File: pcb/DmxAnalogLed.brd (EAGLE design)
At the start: 37 parts, among them J1 RS485, J2 POWER_JACKPTH, J3 RS485, Q1 16MHz 10ppm, U1 ARDUINO_LEONARDO-REV3B_SMARTP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, U2 SN75176ASOIC, X1 USBPTH

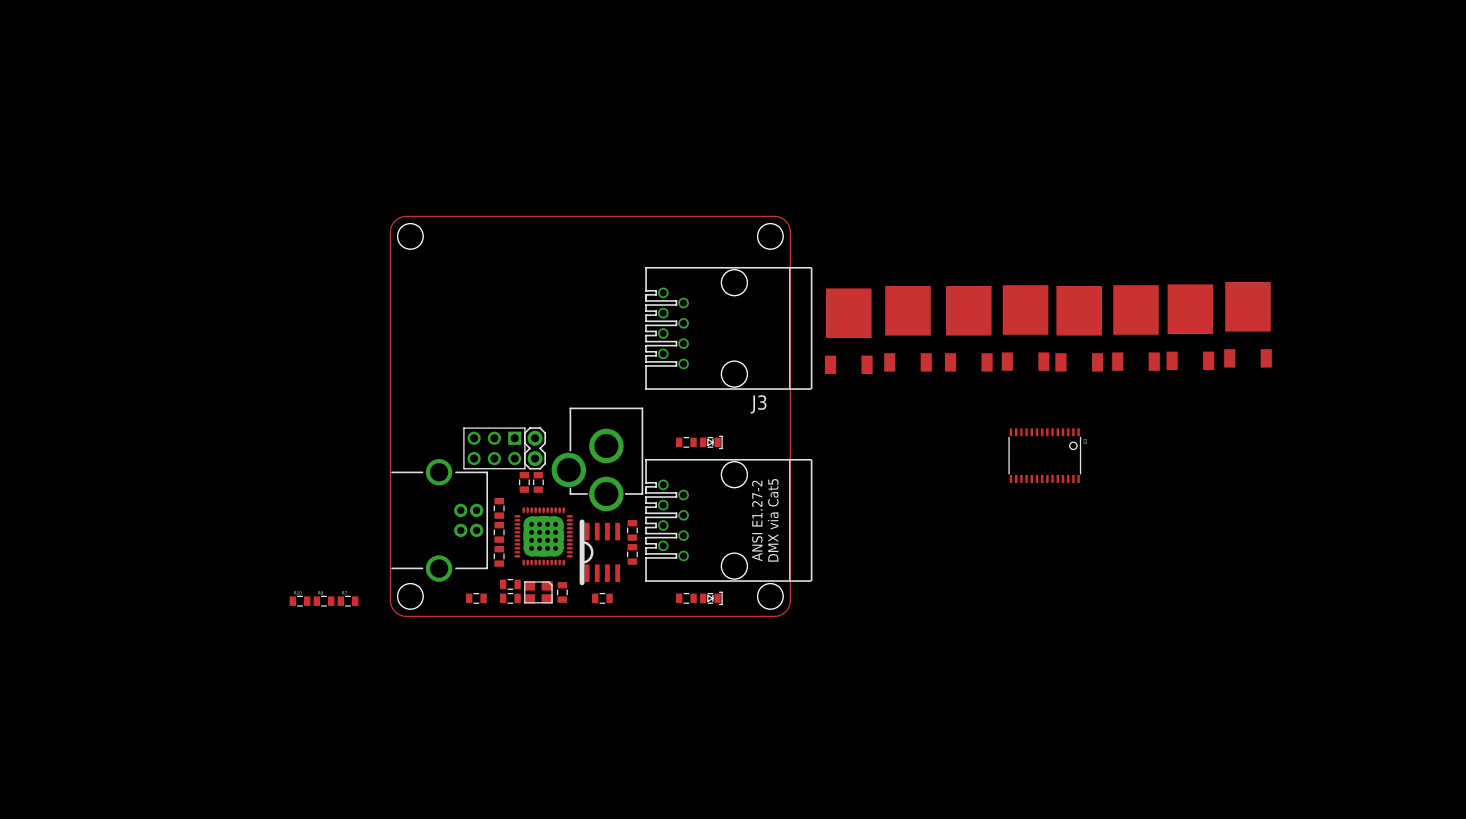
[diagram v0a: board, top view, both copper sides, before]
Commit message: Add isolated RS485 circuit, begin transistor layout
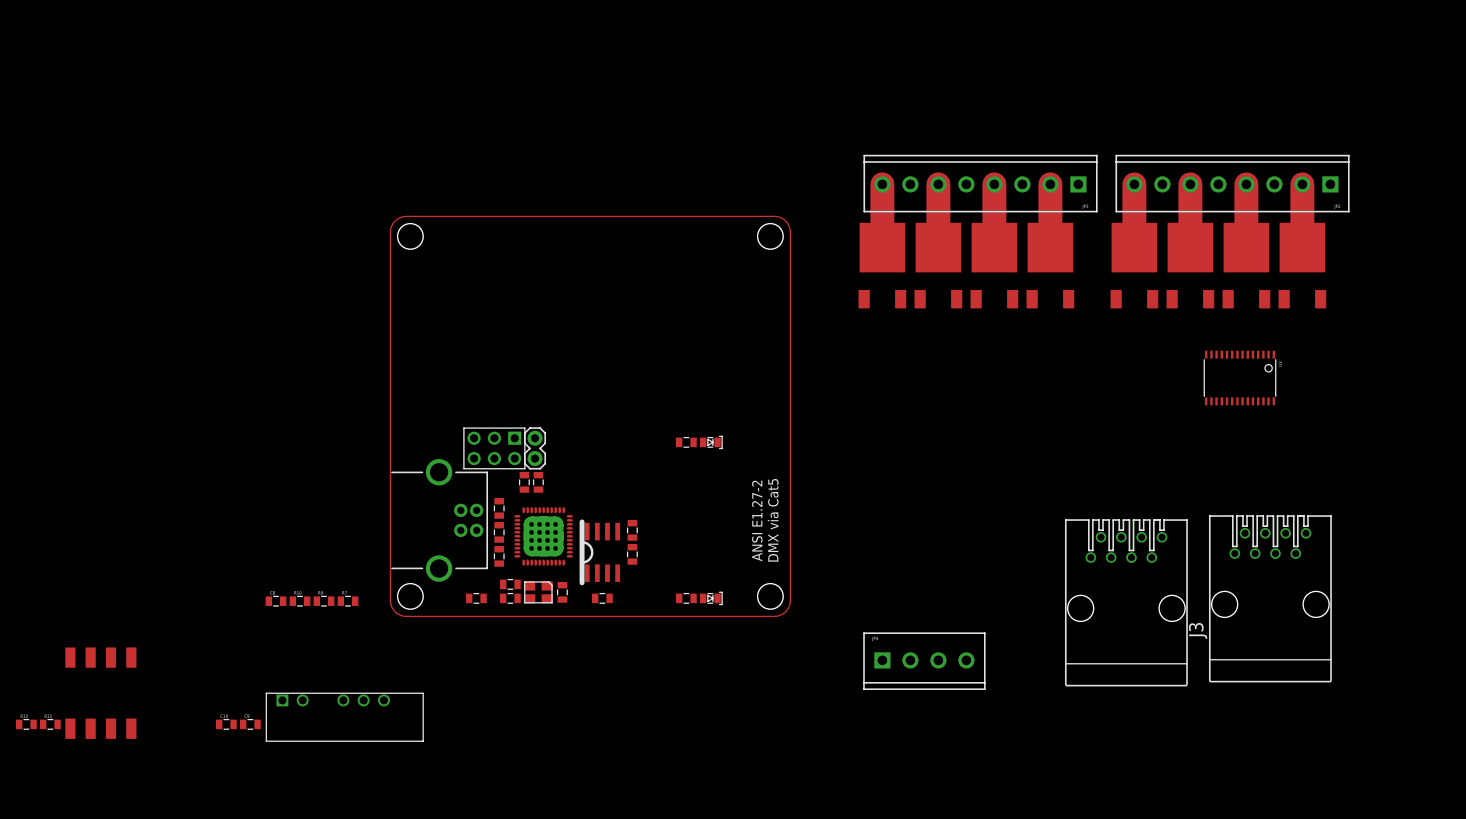
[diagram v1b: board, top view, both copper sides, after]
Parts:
- removed J2: POWER_JACKPTH, SparkFun:POWER_JACK_PTH
- added C10: 10uF, SparkFun:0805
- added C8: 100nF, SparkFun:0805
- added C9: 4.7uF, SparkFun:0805
- added JP2, JP3: (no value), SparkFun:SCREWTERMINAL-3.5MM-8
- added JP4: (no value), SparkFun:SCREWTERMINAL-3.5MM-4
- added R11, R12: 470, SparkFun:0805
- added U$10: DC_DC_ISOLATED_0505, blinkiverse:IB_XLS-1W
- added U$12: 6N137, sonos_library:8_SOIC
- moved J3 75.4 mm to (110.0, 1.50), turned to 0 degrees
- moved J1 50.2 mm to (92.0, 1.00), turned to 0 degrees
- moved U3 26.3 mm to (106.2, 29.8)
- moved U$5 10.5 mm to (93.0, 43.0)
- moved U$3 10.4 mm to (107.0, 43.0)
- moved U$4 10.3 mm to (100.0, 43.0)
- moved U$1 10.0 mm to (114.0, 43.0)
- moved U$9 9.21 mm to (61.5, 43.0)
- moved U$8 8.77 mm to (68.5, 43.0)
- moved U$7 8.52 mm to (75.5, 43.0)
- moved U$6 8.39 mm to (82.5, 43.0)
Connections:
- new net 5V_ISO: C10.2, C7.2, U$10.P$5, U$12.P$2, U2.8
- new net GND_ISO: C10.1, C7.1, J1.7, J1.8, J3.7, J3.8, R2.2, U$10.P$3, U$10.P$4, U2.5
- new net N$10: JP4.1, JP4.2
- new net N$13: JP4.3, JP4.4
- new net N$14: R11.1, U$12.P$3
- new net RX_ISO: R11.2, U2.1
- new net V_LED: JP2.1, JP2.3, JP2.5, JP2.7, JP3.1, JP3.3, JP3.5, JP3.7
- net GND: now also C8.1, C9.1, U$10.P$2, U$12.P$5; no longer C7.1, J1.7, J1.8, J2.GND, J2.GNDBREAK, J3.7, J3.8, R2.2, U2.5, U3.2
- net OUT0: now also JP2.2
- net OUT1: now also JP2.4
- net OUT2: now also JP2.6
- net OUT3: now also JP2.8
- net OUT4: now also JP3.2
- net OUT5: now also JP3.4
- net OUT6: now also JP3.6
- net OUT7: now also JP3.8
- net RX: no longer U2.1
- net TX: now also R12.1, U$12.P$6; no longer U2.4
- net VCC: now also C8.2, C9.2, R12.2, U$10.P$1, U$12.P$8, U3.2; no longer C7.2, U2.8
- net VMOT: no longer J2.PWR
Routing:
- net OUT7: track 0.00 -> 7.90 mm
- net OUT6: track 0.00 -> 7.90 mm
- net OUT5: track 0.00 -> 7.90 mm
- net OUT4: track 0.00 -> 7.90 mm
- net OUT3: track 0.00 -> 7.90 mm
- net OUT2: track 0.00 -> 7.90 mm
- net OUT1: track 0.00 -> 7.90 mm
- net OUT0: track 0.00 -> 7.90 mm

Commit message: Board update
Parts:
- moved R12 155.2 mm to (107.0, 15.5), turned to 90 degrees
- moved R11 151.7 mm to (107.0, 12.0), turned to 90 degrees
- moved U$12 151.3 mm to (109.5, 11.5)
- moved C10 117.8 mm to (93.5, 16.0)
- moved C9 104.7 mm to (83.0, 16.0), turned to 180 degrees
- moved U$10 98.5 mm to (82.0, 13.5)
- moved C7 88.2 mm to (106.2, 8.00), turned to 180 degrees
- moved R2 77.4 mm to (102.0, 19.2)
- moved U2 76.2 mm to (102.5, 13.5), turned to 180 degrees
- moved R1 72.5 mm to (102.8, 8.25), turned to 0 degrees
- moved C5 9.90 mm to (23.2, 17.8), turned to 180 degrees
- moved J3 6.02 mm to (109.5, -4.50)
- moved J1 5.50 mm to (92.0, -4.50)

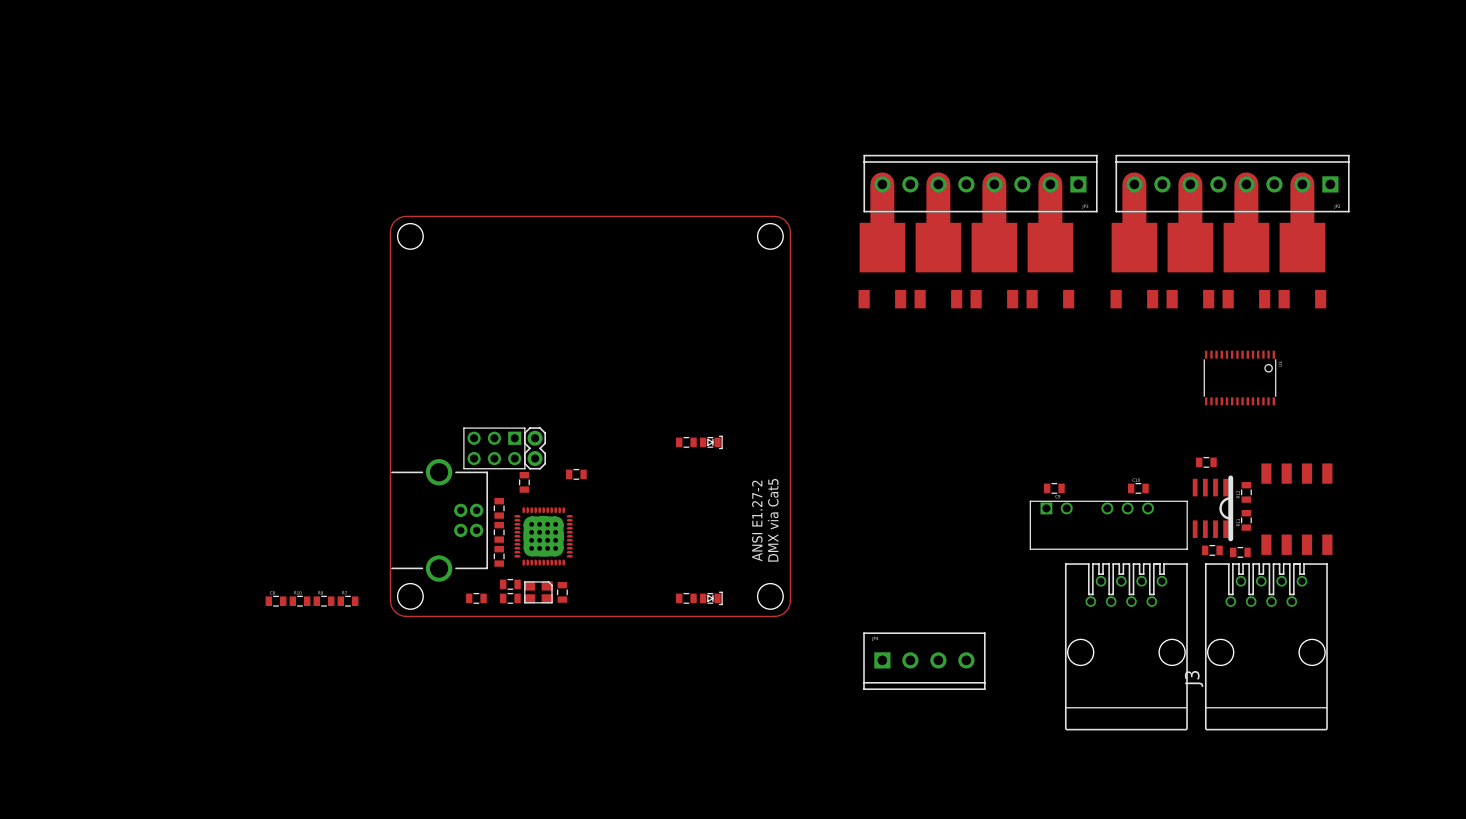
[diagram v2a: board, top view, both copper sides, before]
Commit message: Remove PWM chip, start routing board
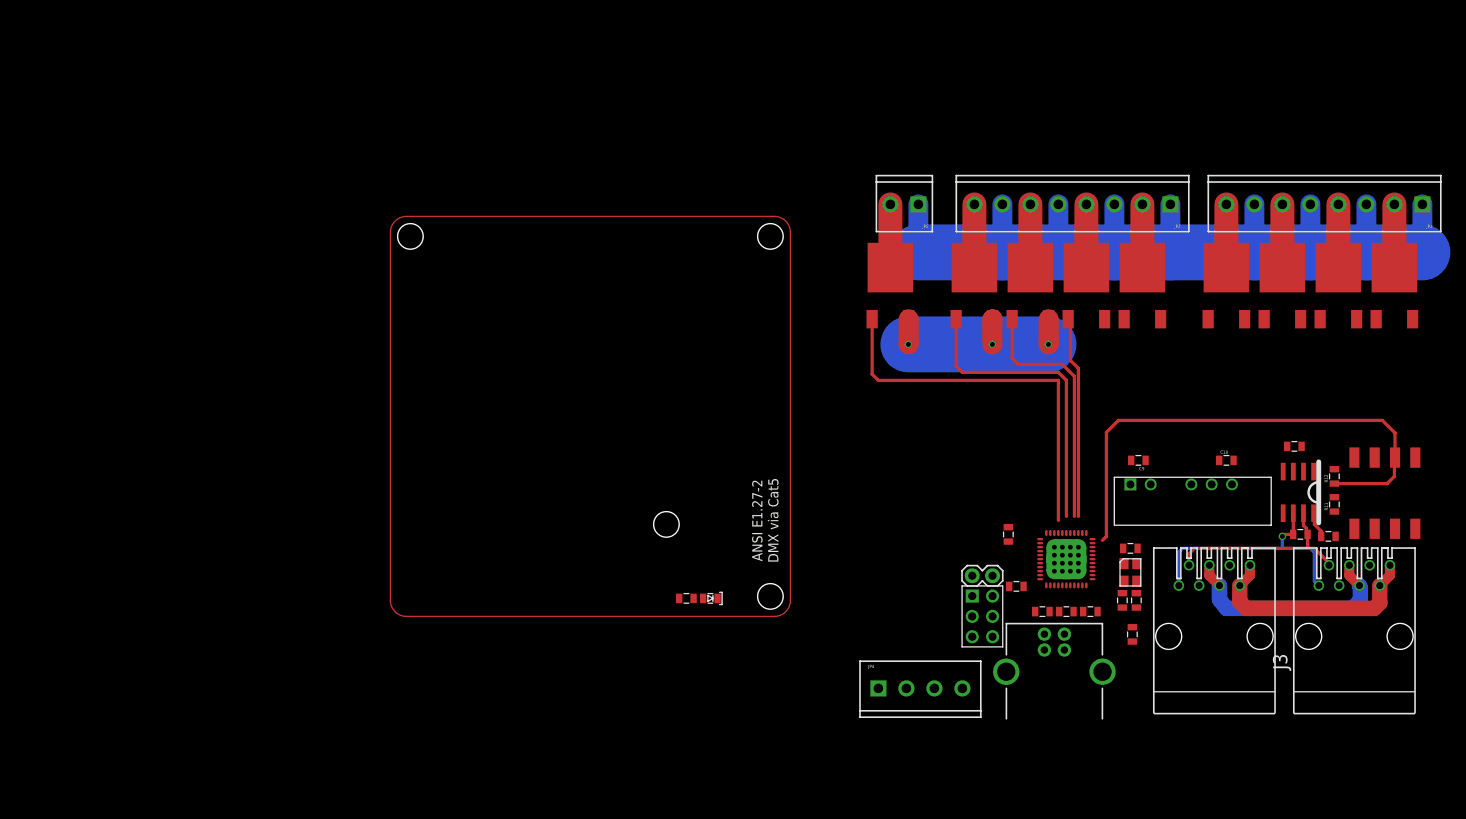
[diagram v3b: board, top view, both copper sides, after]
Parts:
- removed C8: 100nF, SparkFun:0805
- removed DEBUG1: GREEN, SparkFun:LED-0805
- removed R10, R7, R9: 10k, SparkFun:0805
- removed R3: 330, SparkFun:0805
- removed U3: (no value), adafruit:TSSOP28
- added JP5: (no value), SparkFun:SCREWTERMINAL-3.5MM-2
- added U$11: N_MOSFET, blinkiverse:TO252
- moved R4 82.1 mm to (92.8, -2.25), turned to 270 degrees
- moved C1 78.3 mm to (93.2, 2.00), turned to 90 degrees
- moved C4 76.5 mm to (91.5, 2.00), turned to 270 degrees
- moved X1 75.9 mm to (83.0, -4.20), turned to 90 degrees
- moved C6 74.2 mm to (87.5, 0.60), turned to 180 degrees
- moved Q1 74.0 mm to (92.5, 5.50), turned to 270 degrees
- moved R5 71.6 mm to (84.5, 0.60), turned to 0 degrees
- moved C2 71.2 mm to (92.5, 8.50), turned to 180 degrees
- moved R6 69.1 mm to (81.5, 0.60), turned to 0 degrees
- moved U1 65.4 mm to (84.5, 7.15), turned to 90 degrees
- moved U$2 64.5 mm to (74.0, 0.00), turned to 0 degrees
- moved C3 62.9 mm to (78.2, 3.75), turned to 0 degrees
- moved JP1 59.0 mm to (75.3, 5.08), turned to 180 degrees
- moved C5 54.5 mm to (77.2, 10.2), turned to 270 degrees
- moved JP2 11.8 mm to (129.0, 51.5)
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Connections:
- removed net D10: R3.2, U1.30
- removed net N$7: DEBUG1.A, R3.1
- removed net PWM_OE: R10.1, U3.23
- removed net SCL: R7.1, U1.18, U3.26
- removed net SDA: R9.1, U1.19, U3.27
- new net OUT8: JP5.2, U$11.P$3
- new net PWM8: U$11.P$1, U1.30
- net D9: no longer U1.29
- net GND: now also U$11.P$2; no longer C8.1, DEBUG1.C, U3.1, U3.14, U3.24, U3.25, U3.3, U3.4, U3.5
- net PWM0: now also U1.18; no longer U3.6
- net PWM1: now also U1.19; no longer U3.7
- net PWM2: now also U1.25; no longer U3.8
- net PWM3: now also U1.22; no longer U3.9
- net PWM4: now also U1.26; no longer U3.10
- net PWM5: now also U1.27; no longer U3.11
- net PWM6: now also U1.28; no longer U3.12
- net PWM7: now also U1.29; no longer U3.13
- net VCC: no longer C8.2, R10.2, R7.2, R9.2, U3.2, U3.28
- net V_LED: now also JP5.1
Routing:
- net V_LED: track 0.00 -> 117.7 mm
- net TX: track 0.00 -> 64.4 mm
- net PWM8: track 0.00 -> 48.0 mm
- net PWM7: track 0.00 -> 37.4 mm
- net RS485A: track 0.00 -> 31.5 mm, vias 0 -> 1
- net PWM6: track 0.00 -> 31.1 mm
- net GND_ISO: track 0.00 -> 28.5 mm
- net VMOT: track 0.00 -> 28.3 mm
- net GND: track 0.00 -> 27.0 mm, vias 0 -> 3
- net PWM5: track 0.00 -> 25.2 mm
- net RS485B: track 0.00 -> 24.9 mm
- net OUT8: track 0.00 -> 7.90 mm
- net 5V_ISO: track 0.00 -> 3.29 mm

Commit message: Start laying out board
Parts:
- moved R4 65.9 mm to (29.0, 14.2)
- moved JP1 62.9 mm to (15.8, 25.3)
- moved U$2 62.9 mm to (14.5, 20.2)
- moved C4 62.7 mm to (31.0, 18.5)
- moved C6 61.7 mm to (27.4, 14.2), turned to 90 degrees
- moved JP2 61.1 mm to (71.0, 70.8)
- moved JP3 61.1 mm to (39.5, 70.8)
- moved JP5 61.1 mm to (8.00, 70.8)
- moved U$1 61.1 mm to (67.5, 59.8)
- moved U$11 61.1 mm to (4.50, 59.8)
- moved U$3 61.1 mm to (60.5, 59.8)
- moved U$4 61.1 mm to (53.5, 59.8)
- moved U$5 61.1 mm to (46.5, 59.8)
- moved U$6 61.1 mm to (36.0, 59.8)
- moved U$7 61.1 mm to (29.0, 59.8)
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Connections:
- removed net N$10: JP4.1, JP4.2
- removed net N$13: JP4.3, JP4.4
- net GND: now also JP4.3, JP4.4
- net PWM2: now also U1.22; no longer U1.25
- net PWM3: now also U1.25; no longer U1.22
- net V_LED: now also JP4.1, JP4.2
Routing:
- net N$7: track 0.00 -> 300.0 mm
- net N$11: track 195.3 -> 0.00 mm
- net GND: track 27.0 -> 172.9 mm, vias 3 -> 10
- net PWM0: track 0.00 -> 71.0 mm
- net V_LED: track 117.7 -> 187.4 mm
- net PWM1: track 0.00 -> 63.5 mm
- net PWM2: track 0.00 -> 54.0 mm
- net PWM3: track 0.00 -> 46.0 mm
- net PWM4: track 0.00 -> 36.0 mm
- net VCC: track 0.00 -> 20.9 mm
- net GND_ISO: track 28.5 -> 42.1 mm
- net TX: track 64.4 -> 54.5 mm, vias 0 -> 2
- net N$14: track 0.00 -> 9.32 mm
- net N$2: track 0.00 -> 6.51 mm
- net PWM5: track 25.2 -> 31.3 mm
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
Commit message: Routed, pending review
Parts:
- removed DEBUG: RED, SparkFun:LED-0805
- removed JP1: (no value), SparkFun:1X02
- added C11: .3uF, SparkFun:0805
- added C12: .1uF, SparkFun:0805
- added C13: .3uF, SparkFun:1210
- added C14: .1uF, SparkFun:1210
- added C15: ?uF, SparkFun:0805
- added C16: 4.7uF, SparkFun:1210
- added C17: 10uF, SparkFun:1210
- added C18, C19, C20, C21: ?uF, SparkFun:1210
- added C8: 1uF, SparkFun:0805
- added IC2: 7805TV, linear:TO220V
- added J2: POWER_JACKPTH, SparkFun:POWER_JACK_PTH
- added JP6: (no value), SparkFun:1X05
- added LED1: (no value), SparkFun:LED5MM
- moved R8 48.1 mm to (40.5, 26.5)
- moved U$2 28.5 mm to (41.8, 11.8)
- moved JP4 17.8 mm to (4.25, 21.8), turned to 270 degrees
- moved R2 12.3 mm to (66.8, 30.2)
- moved J1 11.6 mm to (56.0, 6.50)
- moved J3 11.6 mm to (73.5, 6.50)
- moved R1 11.6 mm to (66.8, 19.2)
- moved R11 11.6 mm to (71.0, 23.0)
- moved R12 11.6 mm to (71.0, 26.5)
- moved U$10 11.6 mm to (64.2, 37.5)
- moved U$12 11.6 mm to (73.5, 22.5)
- moved U2 11.6 mm to (66.5, 24.5)
- moved C7 11.5 mm to (70.2, 19.2)
- moved C6 11.3 mm to (38.1, 17.5), turned to 270 degrees
- moved R4 11.2 mm to (39.8, 17.5)
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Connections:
- removed net AREF: U1.42
- removed net D9: R8.2
- removed net V_LED: JP2.1, JP2.3, JP2.5, JP2.7, JP3.1, JP3.3, JP3.5, JP3.7, JP4.1, JP4.2, JP5.1
- new net A1: JP6.2, U1.37
- new net LED: R8.2, U1.31
- new net N$10: C8.2, U1.7, X1.VBUS
- new net N$11: C15.2, U1.42
- new net V_PWM: C11.2, C13.1, C18.1, C19.1, C20.1, C21.1, IC2.1, J2.PWR, JP2.1, JP2.3, JP2.5, JP2.7, JP3.1, JP3.3, JP3.5, JP3.7, JP4.1, JP4.2, JP5.1
- net 5V_ISO: now also C17.1
- net A2: now also JP6.3; no longer JP1.2
- net A3: now also JP6.4; no longer JP1.1
- net GND: now also C11.1, C12.1, C13.2, C14.2, C15.1, C16.2, C18.2, C19.2, C20.2, C21.2, C8.1, IC2.2, J2.GND, J2.GNDBREAK, JP6.5, LED1.K; no longer DEBUG.C
- net GND_ISO: now also C17.2
- net N$8: now also LED1.A; no longer DEBUG.A
- net VCC: now also C12.2, C14.1, C16.1, IC2.3, JP6.1; no longer U1.7, X1.VBUS
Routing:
- net V_PWM: track 0.00 -> 237.5 mm, vias 0 -> 4
- net GND: track 172.9 -> 403.3 mm, vias 10 -> 18
- net V_LED: track 187.4 -> 0.00 mm
- net VCC: track 20.9 -> 149.5 mm, vias 0 -> 3
- net GND_ISO: track 42.1 -> 87.1 mm, vias 0 -> 2
- net 5V_ISO: track 6.56 -> 37.7 mm, vias 0 -> 1
- net N$8: track 0.00 -> 25.4 mm
- net RESET: track 0.00 -> 17.5 mm, vias 0 -> 1
- net N$7: track 300.0 -> 317.0 mm
- net LED: track 0.00 -> 14.5 mm, vias 0 -> 2
- net N$10: track 0.00 -> 12.9 mm
- net MOSI: track 0.00 -> 12.0 mm
- net SCK: track 0.00 -> 10.1 mm
- net A3: track 0.00 -> 7.98 mm
- net MISO: track 0.00 -> 7.82 mm
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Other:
- board text added: "Analog LED Fader"
- board text removed: "ANSI E1.27-2"
- board text removed: "DMX via Cat5"
- board text removed: "USB-DMX"

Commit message: Re-wire PWMs for hardware PWM generation. Bugfix: Serial should be connected to AVR RX, not TX
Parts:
- removed JP5: (no value), SparkFun:SCREWTERMINAL-3.5MM-2
- removed U$11: N_MOSFET, blinkiverse:TO252
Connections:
- removed net OUT8: JP5.2, U$11.P$3
- removed net PWM8: U$11.P$1, U1.30
- removed net TX: R12.1, U$12.P$6, U1.21
- net GND: no longer U$11.P$2
- net LED: now also U1.18; no longer U1.31
- net PWM0: now also U1.12; no longer U1.18
- net PWM1: now also U1.27; no longer U1.19
- net PWM2: now also U1.29; no longer U1.22
- net PWM3: now also U1.30; no longer U1.25
- net PWM4: now also U1.31; no longer U1.26
- net PWM5: now also U1.32; no longer U1.27
- net PWM6: now also U1.25; no longer U1.28
- net PWM7: now also U1.26; no longer U1.29
- net RX: now also R12.1, U$12.P$6
- net V_PWM: no longer JP5.1
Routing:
- net RX: track 0.00 -> 53.2 mm, vias 0 -> 2
- net TX: track 53.1 -> 0.00 mm, vias 2 -> 0
- net PWM8: track 52.9 -> 0.00 mm
- net GND: track 403.3 -> 392.6 mm, vias 18 -> 17
- net OUT8: track 7.90 -> 0.00 mm
- net LED: track 14.5 -> 7.09 mm, vias 2 -> 0
- net V_PWM: track 237.5 -> 231.5 mm
- net PWM6: track 38.0 -> 42.0 mm, vias 0 -> 2
- net PWM1: track 65.7 -> 61.8 mm
- net PWM0: track 73.2 -> 75.5 mm, vias 0 -> 2
- net PWM7: track 43.8 -> 45.4 mm, vias 0 -> 2
- net PWM4: track 34.5 -> 36.0 mm
- net PWM3: track 48.0 -> 49.1 mm
- net VCC: track 149.5 -> 150.5 mm

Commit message: Almost ready for a re-release of RevA
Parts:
- added R10, R13, R14, R15, R16, R3, R7, R9: 10K, SparkFun:0805
- added R17, R18, R19, R20, R21, R22, R23, R24: 50, SparkFun:0805
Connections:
- new net PWM0_MID: R10.2, R17.1, U$1.P$1
- new net PWM1_MID: R19.1, R9.2, U$3.P$1
- new net PWM2_MID: R20.1, R7.2, U$4.P$1
- new net PWM3_MID: R21.1, R3.2, U$5.P$1
- new net PWM4_MID: R13.2, R18.1, U$6.P$1
- new net PWM5_MID: R14.2, R22.1, U$7.P$1
- new net PWM6_MID: R15.2, R23.1, U$8.P$1
- new net PWM7_MID: R16.2, R24.1, U$9.P$1
- net GND: now also R10.1, R13.1, R14.1, R15.1, R16.1, R3.1, R7.1, R9.1
- net PWM0: now also R17.2; no longer U$1.P$1
- net PWM1: now also R19.2; no longer U$3.P$1
- net PWM2: now also R20.2; no longer U$4.P$1
- net PWM3: now also R21.2; no longer U$5.P$1
- net PWM4: now also R18.2; no longer U$6.P$1
- net PWM5: now also R22.2; no longer U$7.P$1
- net PWM6: now also R23.2; no longer U$8.P$1
- net PWM7: now also R24.2; no longer U$9.P$1
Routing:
- net GND: track 392.6 -> 405.4 mm
- net PWM6: track 42.0 -> 34.2 mm
- net PWM7: track 45.4 -> 38.9 mm
- net PWM7_MID: track 0.00 -> 4.97 mm
- net PWM6_MID: track 0.00 -> 4.97 mm
- net PWM5_MID: track 0.00 -> 4.97 mm
- net PWM4_MID: track 0.00 -> 4.97 mm
- net PWM3_MID: track 0.00 -> 4.97 mm
- net PWM2_MID: track 0.00 -> 4.97 mm
- net PWM1_MID: track 0.00 -> 4.97 mm
- net PWM0_MID: track 0.00 -> 4.97 mm
- net PWM5: track 31.6 -> 29.0 mm
- net PWM0: track 75.5 -> 73.8 mm
- net PWM2: track 55.7 -> 54.6 mm
- net PWM4: track 36.0 -> 35.0 mm
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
